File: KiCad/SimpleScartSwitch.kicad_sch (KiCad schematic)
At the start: 4 parts, among them CN1 SCART-F, CN2 SCART-F, J1 Conn_02x04_Odd_Even, SW1 SW_8PDT

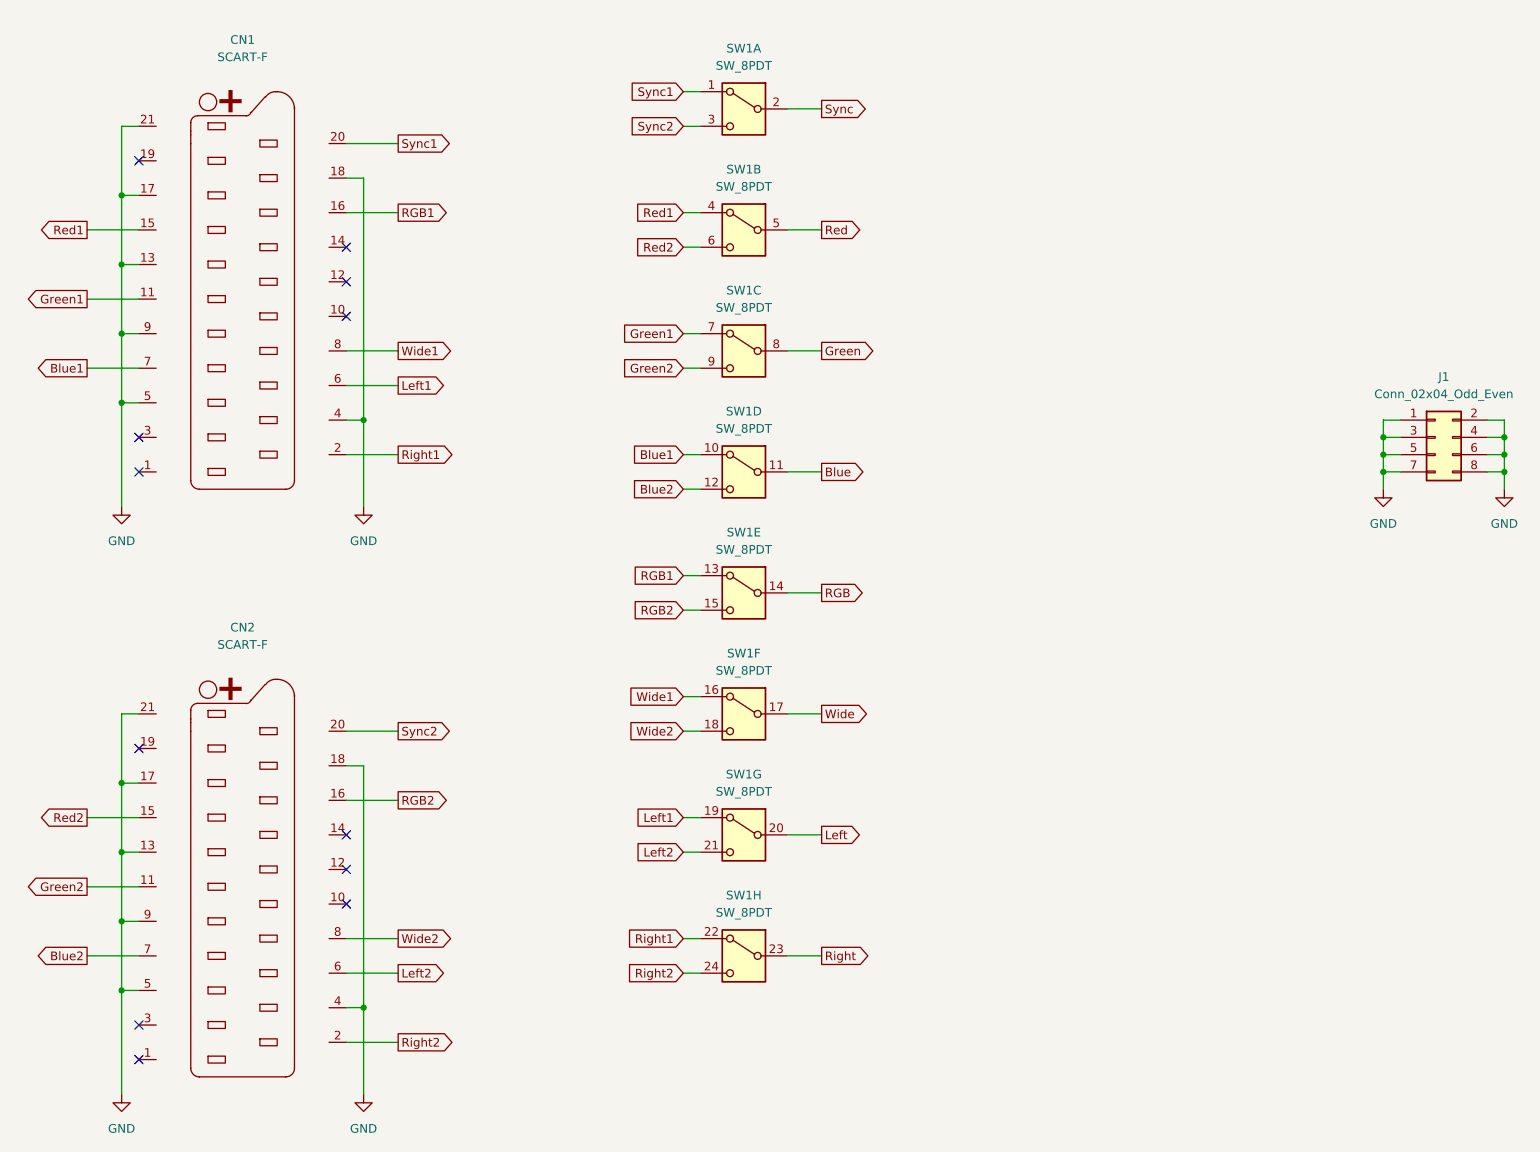
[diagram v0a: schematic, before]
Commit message: SCART plugs can be soldered directly to the board
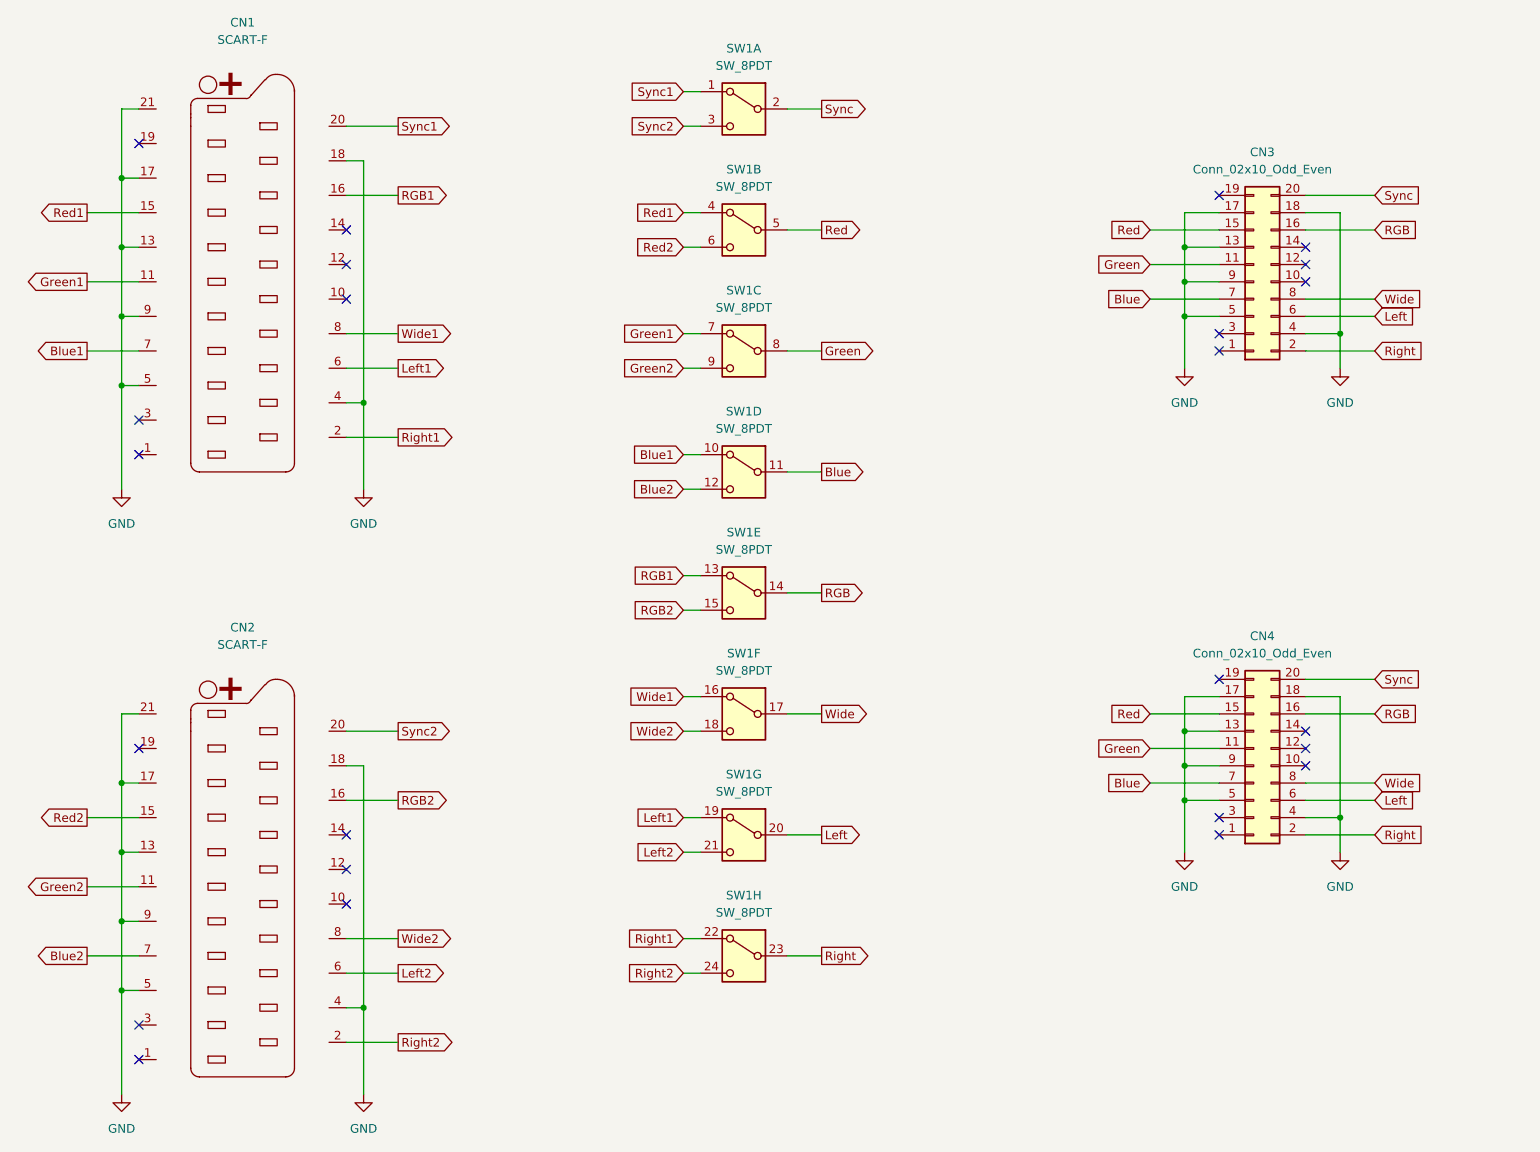
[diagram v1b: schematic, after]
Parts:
- removed J1: Conn_02x04_Odd_Even, Connector_PinHeader_2.54mm:PinHeader_2x04_P2.54mm_Vertical, symbol Connector_Generic:Conn_02x04_Odd_Even
- added CN3, CN4: Conn_02x10_Odd_Even, Library:SCART_Plug, symbol Connector_Generic:Conn_02x10_Odd_Even
- CN1, CN2: footprint Library:SCART -> Library:SCART_Socket
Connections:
- net Blue: now also CN3.7 (Pin_7), CN4.7 (Pin_7)
- net GND: now also CN3.13 (Pin_13), CN3.17 (Pin_17), CN3.18 (Pin_18), CN3.4 (Pin_4), CN3.5 (Pin_5), CN3.9 (Pin_9), CN4.13 (Pin_13), CN4.17 (Pin_17), CN4.18 (Pin_18), CN4.4 (Pin_4), CN4.5 (Pin_5), CN4.9 (Pin_9)
- net Green: now also CN3.11 (Pin_11), CN4.11 (Pin_11)
- net Left: now also CN3.6 (Pin_6), CN4.6 (Pin_6)
- net RGB: now also CN3.16 (Pin_16), CN4.16 (Pin_16)
- net Red: now also CN3.15 (Pin_15), CN4.15 (Pin_15)
- net Right: now also CN3.2 (Pin_2), CN4.2 (Pin_2)
- net Sync: now also CN3.20 (Pin_20), CN4.20 (Pin_20)
- net Wide: now also CN3.8 (Pin_8), CN4.8 (Pin_8)
- no-connect marks 12 -> 24
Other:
- moved on the sheet: CN1
